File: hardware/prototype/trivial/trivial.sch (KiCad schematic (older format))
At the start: 6 parts

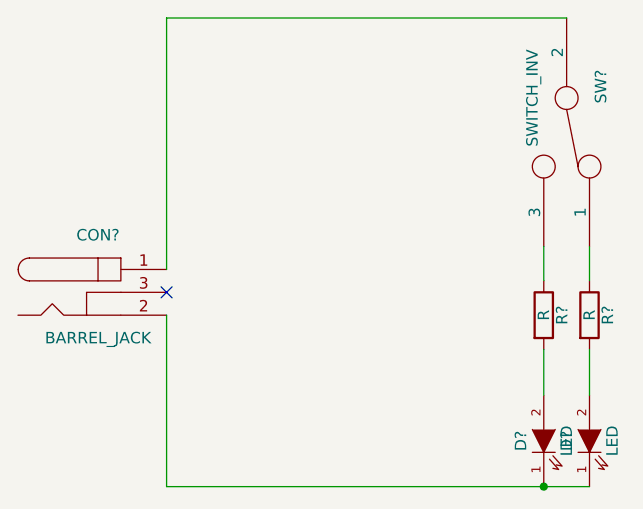
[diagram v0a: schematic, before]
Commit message: Autoroute pi_connect project, add gerber and drill files plotted with default settings.
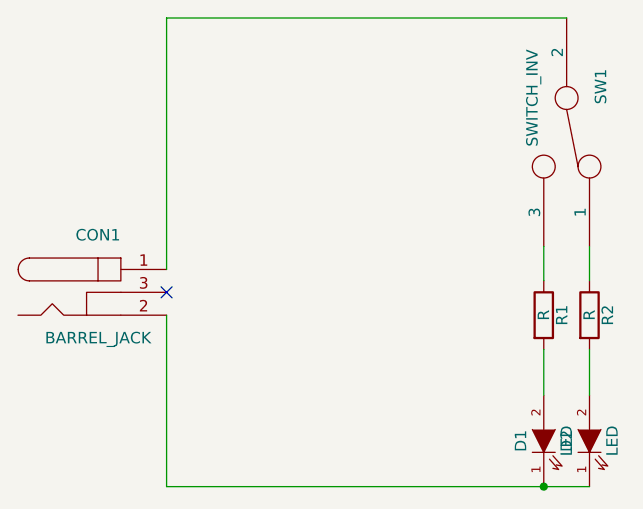
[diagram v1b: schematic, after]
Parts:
- CON1: renamed from CON?; footprint (none) -> Connect:BARREL_JACK
- D1, D2: renamed from D?; footprint (none) -> LEDs:LED-5MM
- R1, R2: renamed from R?; footprint (none) -> Resistors_ThroughHole:Resistor_Horizontal_RM10mm
- SW1: renamed from SW?; footprint (none) -> myparts:SW_SPDT
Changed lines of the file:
@@
 $EndDescr
 $Comp
-L BARREL_JACK CON?
+L BARREL_JACK CON1
 U 1 1 5798A4FF
 P 4550 1900
-F 0 "CON?" H 4550 2150 50  0000 C CNN
+F 0 "CON1" H 4550 2150 50  0000 C CNN
 F 1 "BARREL_JACK" H 4550 1700 50  0000 C CNN
-F 2 "" H 4550 1900 50  0000 C CNN
+F 2 "Connect:BARREL_JACK" H 4550 1900 50  0001 C CNN
 F 3 "" H 4550 1900 50  0000 C CNN
 	1    4550 1900
@@
 $EndComp
 $Comp
-L R R?
+L R R1
 U 1 1 5798A51E
 P 6500 2000
-F 0 "R?" V 6580 2000 50  0000 C CNN
+F 0 "R1" V 6580 2000 50  0000 C CNN
 F 1 "R" V 6500 2000 50  0000 C CNN
-F 2 "" V 6430 2000 50  0000 C CNN
+F 2 "Resistors_ThroughHole:Resistor_Horizontal_RM10mm" V 6430 2000 50  0001 C CNN
 F 3 "" H 6500 2000 50  0000 C CNN
 	1    6500 2000
@@
 $EndComp
 $Comp
-L LED D?
+L LED D1
 U 1 1 5798A547
 P 6500 2550
-F 0 "D?" H 6500 2650 50  0000 C CNN
+F 0 "D1" H 6500 2650 50  0000 C CNN
 F 1 "LED" H 6500 2450 50  0000 C CNN
-F 2 "" H 6500 2550 50  0000 C CNN
+F 2 "LEDs:LED-5MM" H 6500 2550 50  0001 C CNN
 F 3 "" H 6500 2550 50  0000 C CNN
 	1    6500 2550
@@
 $EndComp
 $Comp
-L SWITCH_INV SW?
+L SWITCH_INV SW1
 U 1 1 5798A57D
 P 6600 1200
-F 0 "SW?" H 6400 1350 50  0000 C CNN
+F 0 "SW1" H 6400 1350 50  0000 C CNN
 F 1 "SWITCH_INV" H 6450 1050 50  0000 C CNN
-F 2 "" H 6600 1200 50  0000 C CNN
+F 2 "myparts:SW_SPDT" H 6600 1200 50  0001 C CNN
 F 3 "" H 6600 1200 50  0000 C CNN
 	1    6600 1200
@@
 $EndComp
 $Comp
-L R R?
+L R R2
 U 1 1 5798A634
 P 6700 2000
-F 0 "R?" V 6780 2000 50  0000 C CNN
+F 0 "R2" V 6780 2000 50  0000 C CNN
 F 1 "R" V 6700 2000 50  0000 C CNN
-F 2 "" V 6630 2000 50  0000 C CNN
+F 2 "Resistors_ThroughHole:Resistor_Horizontal_RM10mm" V 6630 2000 50  0001 C CNN
 F 3 "" H 6700 2000 50  0000 C CNN
 	1    6700 2000
@@
 $EndComp
 $Comp
-L LED D?
+L LED D2
 U 1 1 5798A63A
 P 6700 2550
-F 0 "D?" H 6700 2650 50  0000 C CNN
+F 0 "D2" H 6700 2650 50  0000 C CNN
 F 1 "LED" H 6700 2450 50  0000 C CNN
-F 2 "" H 6700 2550 50  0000 C CNN
+F 2 "LEDs:LED-5MM" H 6700 2550 50  0001 C CNN
 F 3 "" H 6700 2550 50  0000 C CNN
 	1    6700 2550
